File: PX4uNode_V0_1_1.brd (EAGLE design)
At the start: 45.4 x 34 mm, 131 parts, among them M3_MOUNT1101 MOUNT-HOLE3.1MM, M3_MOUNT1102 MOUNT-HOLE3.1MM, M3_MOUNT1103 MOUNT-HOLE3.1MM, M3_MOUNT1104 MOUNT-HOLE3.1MM, U101 STM32F4X7VX, U401 MAX3051, U402 MAX3051, X101 3.2x2.5 mm / 24 MHz / 15 ppm

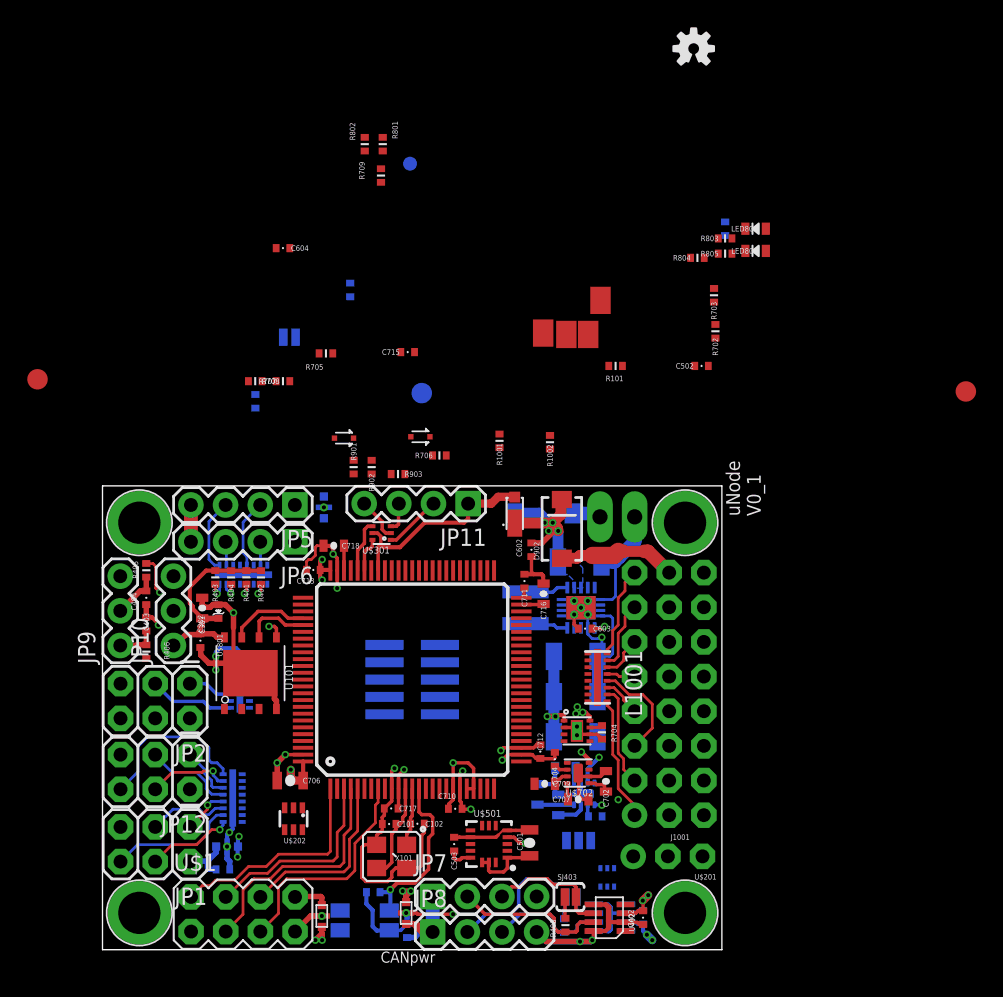
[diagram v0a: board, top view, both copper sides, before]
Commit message: uNode - Lots more layout
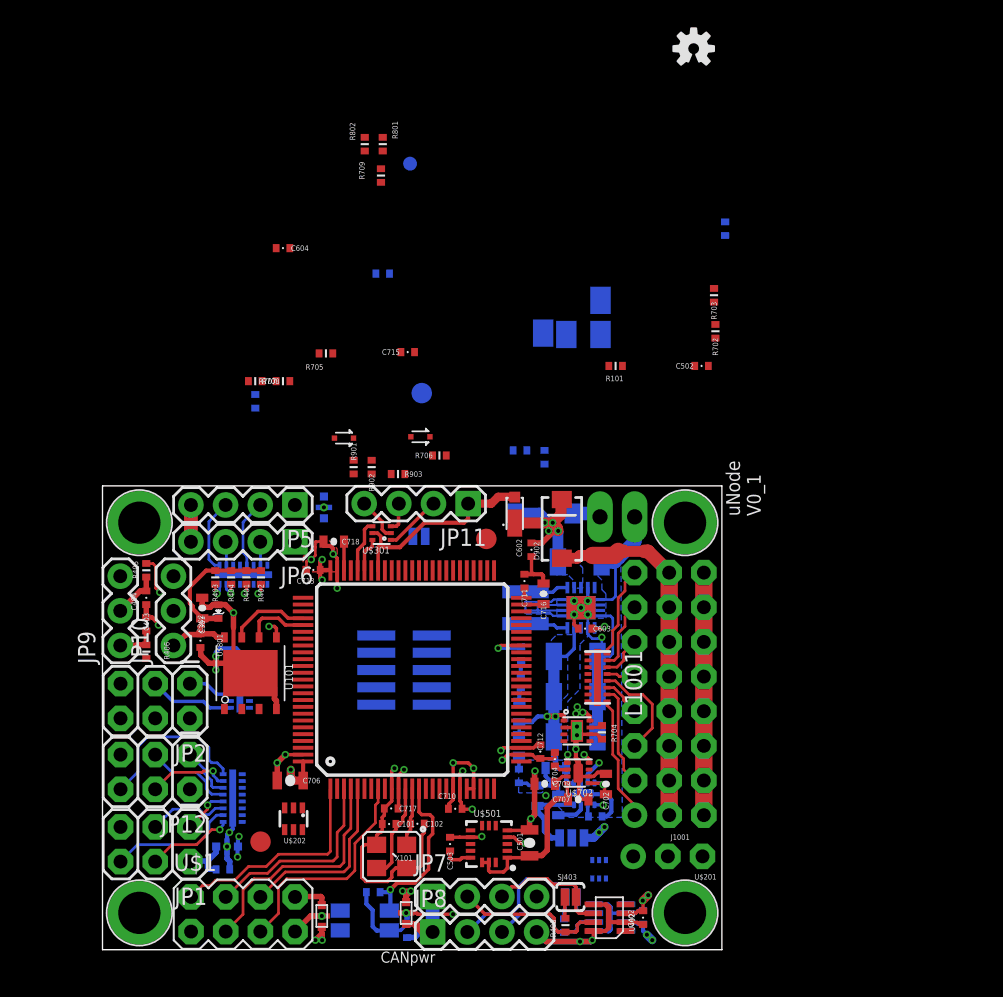
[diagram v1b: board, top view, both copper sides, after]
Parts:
- moved JP1104 61.3 mm to (24.4, 12.1)
- moved R805 41.2 mm to (43.3, 16.9), flipped to the bottom, turned to 90 degrees
- moved LED802 40.2 mm to (43.3, 19.2), flipped to the bottom, turned to 90 degrees
- moved LED801 39.4 mm to (43.3, 21.6), flipped to the bottom, turned to 270 degrees
- moved R803 35.8 mm to (43.5, 23.9), flipped to the bottom, turned to 270 degrees
- moved JP1103 34.9 mm to (40.9, 34.3)
- moved R804 31.8 mm to (43.5, 25.9), flipped to the bottom, turned to 270 degrees
- moved JP202 17.4 mm to (36.0, 34.5), turned to 180 degrees
- moved R701 2.66 mm to (33.3, 53.8), turned to 180 degrees
- moved R1001 1.66 mm to (43.4, 40.8), flipped to the bottom, turned to 180 degrees
- moved R1002 1.17 mm to (45.2, 40.3), flipped to the bottom
- moved JX301 0.92 mm to (34.9, 24.7)
- moved JP1001 0.90 mm to (49.3, 49.3), flipped to the bottom
- moved U$3 0.85 mm to (49.2, 10.1)
- moved C701 0.70 mm to (46.0, 17.5)
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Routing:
- net GND: track 155.6 -> 199.7 mm, vias 17 -> 22
- net V_SERVO: track 8.72 -> 26.5 mm
- net VDD_5V_PERIPH: track 6.60 -> 19.3 mm, vias 9 -> 11
- net VDD_5V: track 10.4 -> 21.1 mm, vias 2 -> 3
- net VDD_3V3_SENSORS: track 6.30 -> 12.6 mm
- net VDD_3V3_SPEKTRUM: track 2.69 -> 6.28 mm
- net !FMU-LED_AMBER: track 0.00 -> 3.51 mm, vias 0 -> 1
- net N$13: track 0.00 -> 1.04 mm
- net N$26: track 0.00 -> 1.03 mm
- net N$7: track 0.00 -> 0.99 mm
- net VDD_3V3_SENSORS_EN: track 0.00 -> 0.61 mm, vias 0 -> 1
- net FMU-VDD_3V3: vias 11 -> 12
- added copper zone on layer 1, net GND
- added copper zone on layer 16, net GND
- added copper zone on layer 16, net VDD_5V

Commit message: Removed unused 3V3 peripheral power from regulator
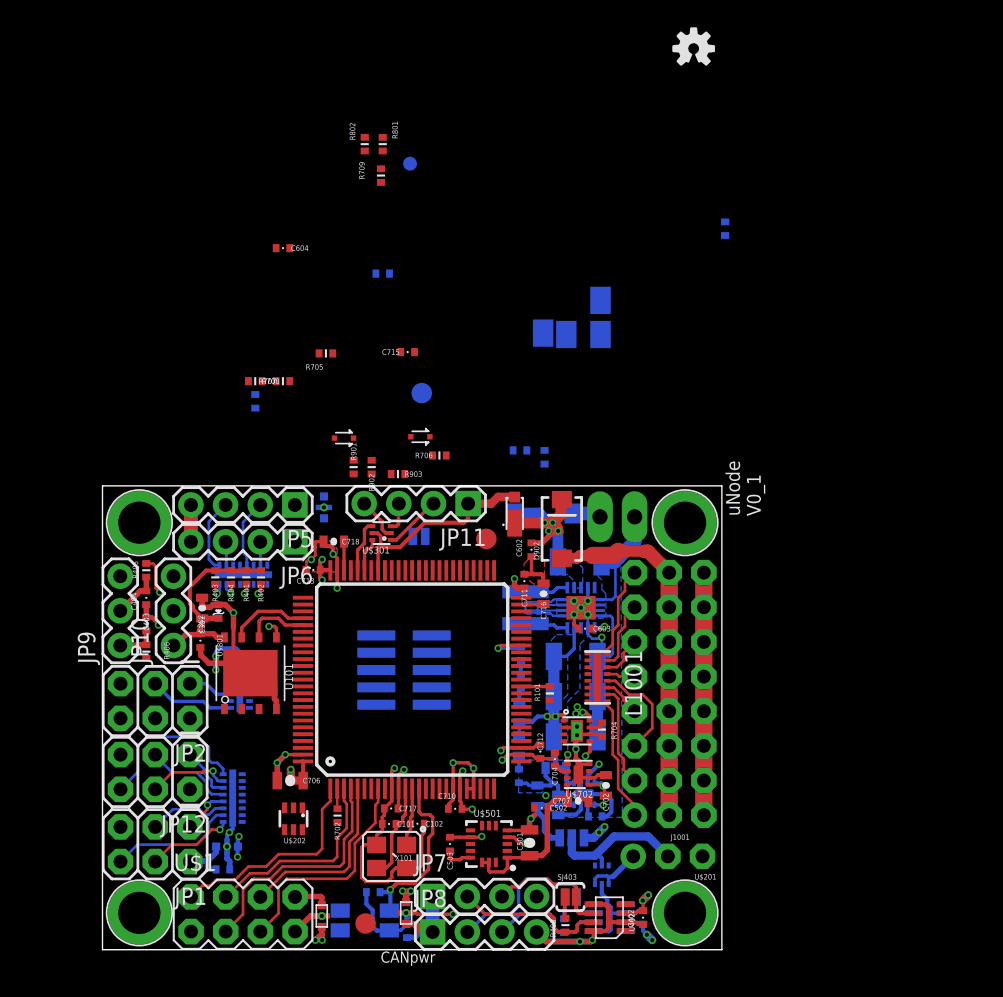
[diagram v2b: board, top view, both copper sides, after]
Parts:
- removed C709: 1u0, pixhawk2:0603-CAP
- removed R703: 10K, pixhawk2:0402-RES
- moved R702 45.0 mm to (30.0, 14.0)
- moved C502 34.4 mm to (45.0, 14.6), turned to 180 degrees
- moved R101 24.5 mm to (45.6, 23.0), turned to 270 degrees
- moved JP1104 9.76 mm to (32.1, 6.12)
- moved U$3 0.45 mm to (49.4, 9.70), turned to 0 degrees
- moved R704 0.20 mm to (49.4, 20.3)
- moved C702 0.10 mm to (49.7, 16.2)
- moved C707 0.10 mm to (47.7, 15.1)
- moved U$702 0.10 mm to (47.7, 17.1)
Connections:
- removed net VDD_3V3_PERIPH: C709.P$1, U$702.7
- removed net VDD_3V3_PERIPH_EN: R703.P$2, U$702.4
- net GND: now also U$702.4; no longer C709.P$2, R703.P$1
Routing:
- net VDD_5V_PERIPH: track 19.3 -> 47.4 mm
- net N$18: track 0.00 -> 10.4 mm
- net N$2: track 0.00 -> 4.44 mm
- net PB2-BOOT1: track 0.00 -> 2.10 mm
- net VDD_3V3_SENSORS_EN: track 0.61 -> 2.19 mm
- net FMU-VDD_3V3: track 42.4 -> 43.7 mm, vias 12 -> 13
- net !VDD_5V_PERIPH_EN: track 0.00 -> 1.23 mm, vias 0 -> 1
- net VDD_3V3_PERIPH: track 1.12 -> 0.00 mm
- net VDD_3V3_PERIPH_EN: track 0.75 -> 0.00 mm, vias 1 -> 0
- net GND: track 199.7 -> 199.1 mm, vias 22 -> 21
- added copper zone on layer 15, net FMU-VDD_3V3

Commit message: uNode - More pullup resistor placed
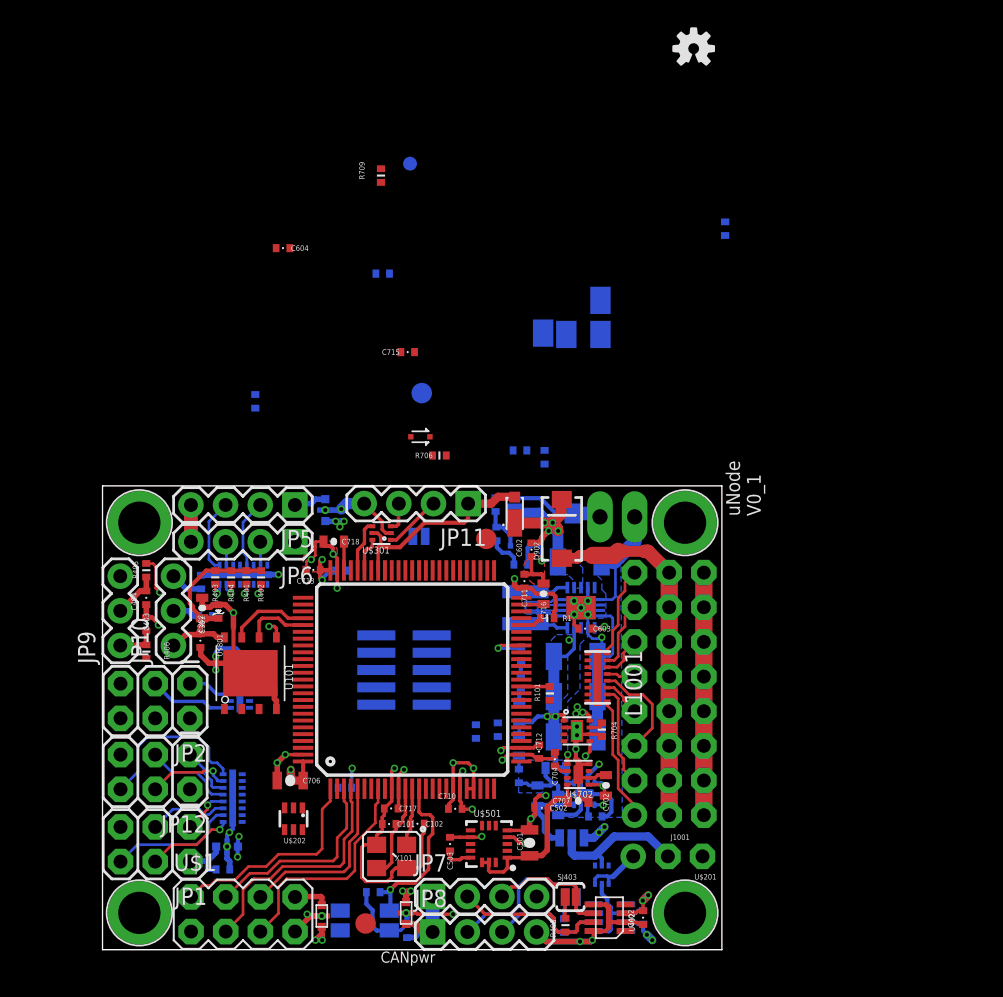
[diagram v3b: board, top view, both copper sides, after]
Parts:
- added R1: 10K, pixhawk2:0402-RES
- moved R801 36.9 mm to (20.4, 28.7), flipped to the bottom, turned to 180 degrees
- moved R802 34.3 mm to (20.0, 31.2), flipped to the bottom, turned to 90 degrees
- moved R708 30.4 mm to (40.2, 20.2), flipped to the bottom, turned to 270 degrees
- moved R707 30.0 mm to (41.8, 20.3), flipped to the bottom, turned to 90 degrees
- moved R705 16.0 mm to (30.4, 32.0), flipped to the bottom, turned to 180 degrees
- moved D1 15.1 mm to (43.4, 33.8), flipped to the bottom
- moved R903 11.2 mm to (43.5, 32.4), flipped to the bottom, turned to 0 degrees
- moved R901 10.8 mm to (41.6, 36.8), flipped to the bottom, turned to 90 degrees
- moved R902 10.4 mm to (41.7, 34.7), flipped to the bottom
- moved R702 2.11 mm to (30.6, 16.1), flipped to the bottom, turned to 0 degrees
- moved L404 0.22 mm to (29.1, 36.4)
- moved C712 0.10 mm to (44.8, 18.7)
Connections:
- removed net !ACCEL_MAG_CS: U101.9
- removed net !VDD_SERVO_VALID: U101.93
- removed net VDD_SERVO_SENS: R902.P$1, R903.P$2
- new net VDD_SERVO_SENSE: R902.P$1, R903.P$2, U101.16
- net !VDD_5V_PERIPH_OC: now also R1.P$2
- net FMU-LED_SAFETY: now also U101.9
- net FMU-VDD_3V3: now also R1.P$1, R705.P$1
- net SAFETY: now also U101.93
- net VDD_5V: no longer R705.P$1
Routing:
- net VDD_5V_PERIPH: track 47.4 -> 90.6 mm, vias 11 -> 14
- net GND: track 199.1 -> 213.6 mm, vias 21 -> 26
- net FMU-VDD_3V3: track 43.7 -> 50.6 mm, vias 13 -> 14
- net V_EXT: track 2.06 -> 8.23 mm
- net IC2_VDD_5V: track 0.00 -> 5.10 mm
- net N$6: track 0.00 -> 3.24 mm
- net VDD_SERVO_SENSE: track 0.00 -> 2.57 mm
- net SAFETY: track 0.00 -> 2.41 mm
- net N$57: track 0.00 -> 2.07 mm
- net !VDD_5V_PERIPH_OC: track 0.00 -> 1.61 mm
- net VDD_3V3_SENSORS_EN: track 2.19 -> 0.71 mm
- net VDD_IN: track 14.4 -> 13.3 mm
- net VDD_5V: vias 3 -> 4

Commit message: PTH for boot and bat
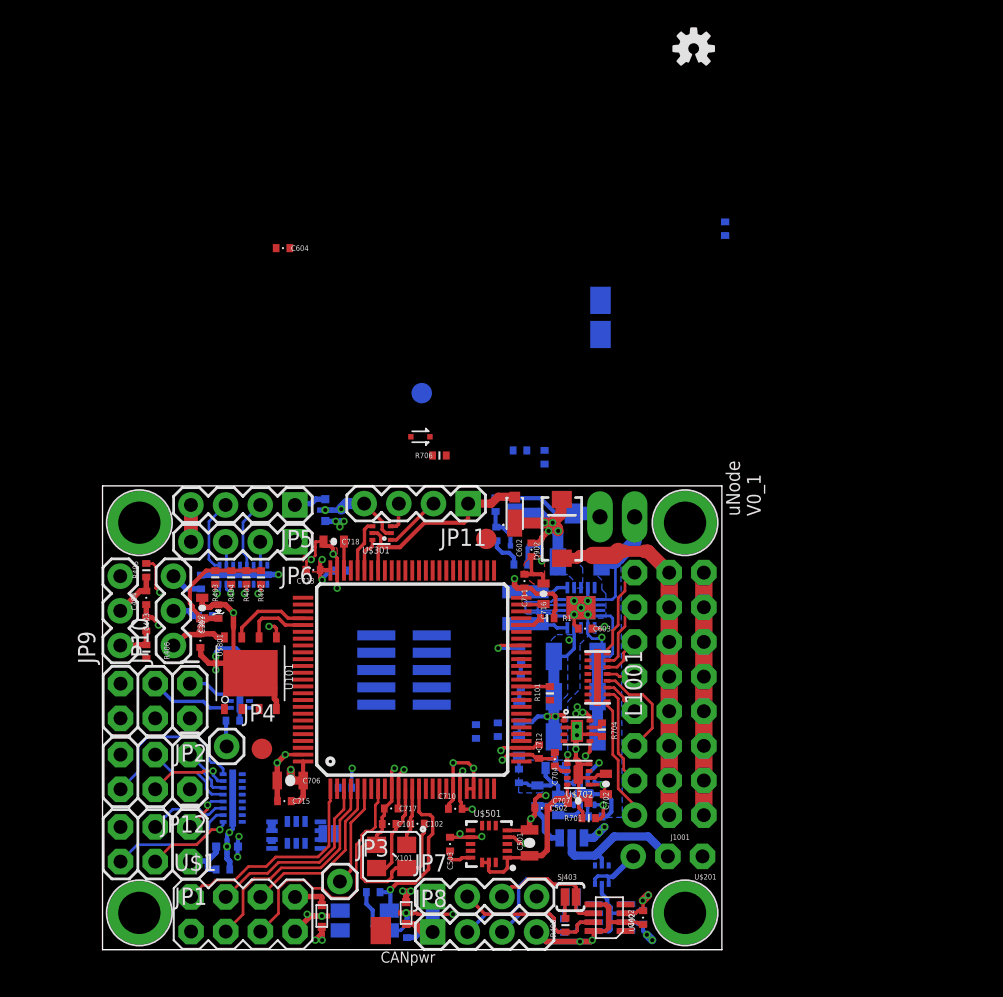
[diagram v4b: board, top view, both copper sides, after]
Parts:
- removed BOOT: PAD.04, pixhawk2:PAD.04X.04
- removed JP701: M01SMD-4.5X1.5, SparkFun-Connectors:PAD-1.5X4.5
- added JP3, JP4: M01PTH, SparkFun-Connectors:1X01
- added U$2: 74LVC2G240-TSSOP-8, pixhawk2:TSSOP8_SOT505-2
- moved JP702 45.8 mm to (33.2, 5.60), flipped to the top
- moved R701 42.7 mm to (48.4, 13.8), flipped to the top, turned to 0 degrees
- moved R709 41.4 mm to (22.4, 21.0), flipped to the bottom, turned to 0 degrees
- moved C715 34.1 mm to (26.1, 15.1), turned to 180 degrees
- moved C201 31.7 mm to (25.2, 12.7), turned to 90 degrees
- moved JP202 22.8 mm to (29.4, 12.7)
- moved JP1104 14.9 mm to (24.5, 18.9)
- moved U$202 1.02 mm to (27.0, 12.8), flipped to the bottom
- moved C702 0.10 mm to (49.7, 16.3)
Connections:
- net FMU-BOOT0: now also JP4.1; no longer BOOT.P$1
- net VBAT: now also JP3.1; no longer JP701.P$1
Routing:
- net VBAT: track 0.00 -> 7.55 mm
- net GND: track 213.6 -> 219.8 mm, vias 26 -> 27
- net FMU-VDD_3V3: track 50.6 -> 52.8 mm
- net GPIO_EXT_1: track 16.6 -> 18.8 mm
- net FMU-BOOT0: track 0.00 -> 1.91 mm
- net VDD_3V3_SPEKTRUM_EN: track 0.65 -> 2.11 mm
- net SPI_EXT_MOSI: track 13.4 -> 12.5 mm
- net SPI_EXT_MISO: track 17.5 -> 16.7 mm
- net !SPI_EXT_NSS: track 14.8 -> 14.1 mm

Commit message: uNode - CAN river 3V3 connected
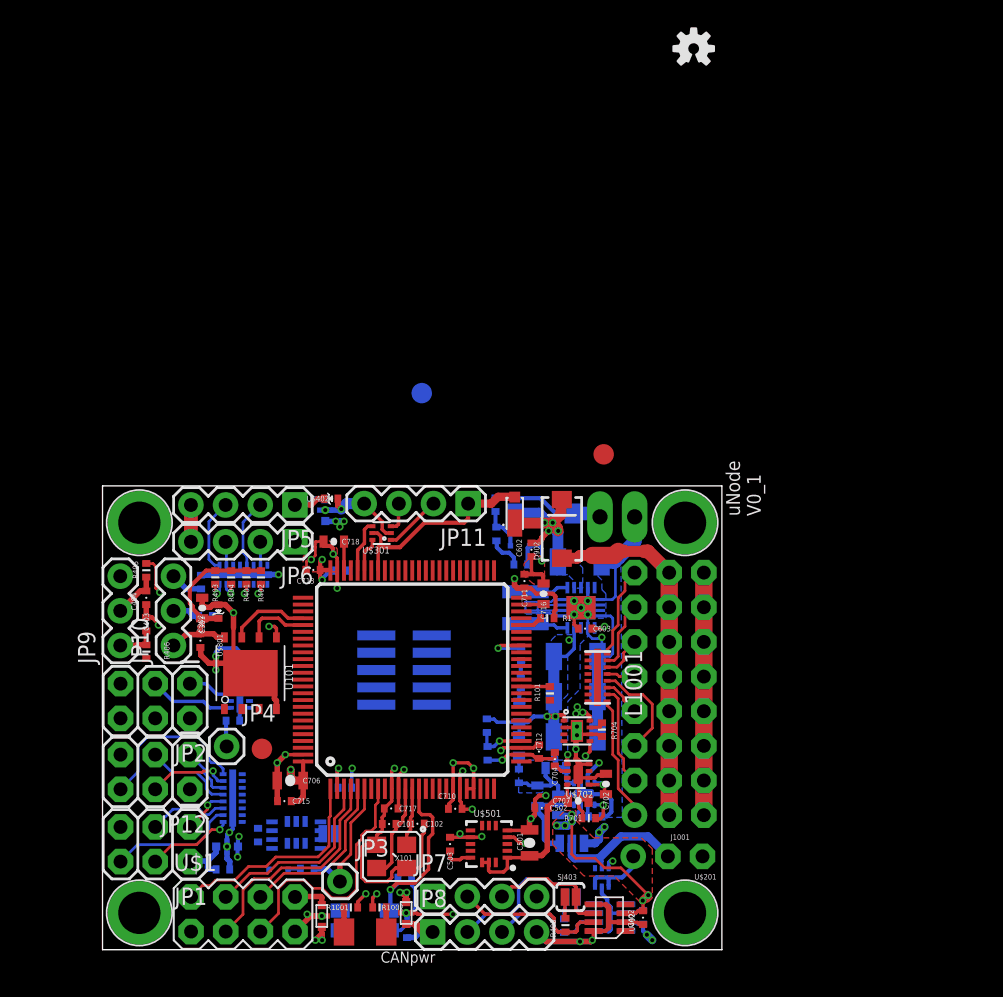
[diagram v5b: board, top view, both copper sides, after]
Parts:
- removed C604: 0u1, pixhawk2:0402-CAP
- removed JP702: M01SMD-4.5X1.5, SparkFun-Connectors:PAD-1.5X4.5
- moved JP1002 48.9 mm to (33.6, 5.50), flipped to the top
- moved JP1001 47.7 mm to (30.5, 5.50), flipped to the top
- moved R1001 35.7 mm to (31.0, 7.30), flipped to the top, turned to 0 degrees
- moved R1002 35.1 mm to (33.1, 7.30), flipped to the top, turned to 180 degrees
- moved U$402 35.0 mm to (29.5, 37.3), flipped to the top, turned to 0 degrees
- moved D2 33.4 mm to (25.7, 10.1), flipped to the bottom, turned to 180 degrees
- moved R706 31.8 mm to (27.8, 10.1), flipped to the bottom
- moved JP1103 10.6 mm to (49.5, 40.5)
- moved C714 2.54 mm to (35.0, 9.48), turned to 0 degrees
- moved R708 1.81 mm to (41.0, 18.6)
- moved C201 1.00 mm to (24.2, 12.6)
- moved R707 0.85 mm to (41.0, 20.6)
- moved JP201 0.40 mm to (47.2, 12.0)
- moved U$3 0.20 mm to (49.4, 9.50)
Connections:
- net GND: no longer C604.P$2, JP702.P$1
- net VDD_5V: no longer C604.P$1
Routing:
- net FMU-VDD_3V3: track 52.8 -> 77.4 mm, vias 14 -> 18
- net VDD_5V_PERIPH: track 90.6 -> 85.4 mm
- net VDD_5V_SENS: track 0.00 -> 3.70 mm, vias 0 -> 1
- net VDD_3V3_SENSORS_EN: track 0.71 -> 3.75 mm, vias 1 -> 2
- net N$28: track 9.43 -> 6.83 mm
- net VDD_5V: track 21.0 -> 23.5 mm
- net IC2_VDD_5V: track 5.10 -> 7.44 mm
- net VBAT: track 7.55 -> 9.82 mm
- net N$23: track 0.00 -> 1.80 mm
- net N$19: track 0.00 -> 1.80 mm
- net FMU-CH9: track 0.00 -> 1.25 mm, vias 0 -> 1
- net FMU-CH10: track 0.00 -> 1.12 mm, vias 0 -> 1
- net N$9: track 0.00 -> 0.92 mm
- net GND: track 219.8 -> 220.7 mm
- net SPEKTRUM_RX: track 0.00 -> 0.77 mm, vias 0 -> 1
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- added copper zone on layer 1, net FMU-VDD_3V3

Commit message: little tweak
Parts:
- moved JP1104 13.5 mm to (11.2, 21.2)
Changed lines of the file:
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@@
 <layer number="13" name="Route13" color="4" fill="5" visible="no" active="no"/>
 <layer number="14" name="Vertical" color="14" fill="15" visible="no" active="yes"/>
-<layer number="15" name="Power" color="11" fill="15" visible="no" active="yes"/>
+<layer number="15" name="Power" color="11" fill="15" visible="yes" active="yes"/>
 <layer number="16" name="Bottom" color="1" fill="1" visible="yes" active="yes"/>
 <layer number="17" name="Pads" color="2" fill="1" visible="yes" active="yes"/>
@@
 <attribute name="BOM" value="EXCLUDE" x="49.53468125" y="40.5136" size="1.778" layer="27" display="off"/>
 </element>
-<element name="JP1104" library="pixhawk2" package="FIDUCIAL-1.5X3" value="FIDUCIAL1.5X3" x="24.4832" y="18.921925">
-<attribute name="PARTNO" value="*" x="24.4832" y="18.921925" size="1.778" layer="27" display="off"/>
-<attribute name="BOM" value="EXCLUDE" x="24.4832" y="18.921925" size="1.778" layer="27" display="off"/>
+<element name="JP1104" library="pixhawk2" package="FIDUCIAL-1.5X3" value="FIDUCIAL1.5X3" x="11.1832" y="21.221925">
+<attribute name="PARTNO" value="*" x="11.1832" y="21.221925" size="1.778" layer="27" display="off"/>
+<attribute name="BOM" value="EXCLUDE" x="11.1832" y="21.221925" size="1.778" layer="27" display="off"/>
 </element>
 <element name="L1001" library="PX4lite" package="DFN16-THIN" value="NUF8402MN" x="49.0848" y="24.1608" rot="R270"/>
